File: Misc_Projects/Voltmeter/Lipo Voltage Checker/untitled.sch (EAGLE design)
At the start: 23 parts, among them IC3 ICL7660CPA

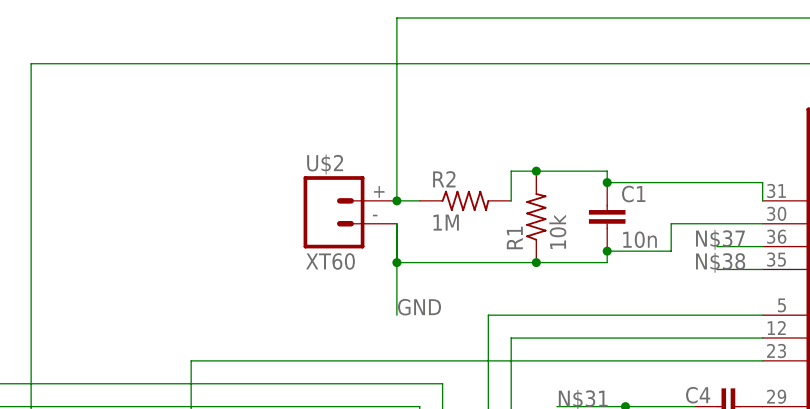
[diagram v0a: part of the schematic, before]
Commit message: Updated to 7mil trace instead of 5mil
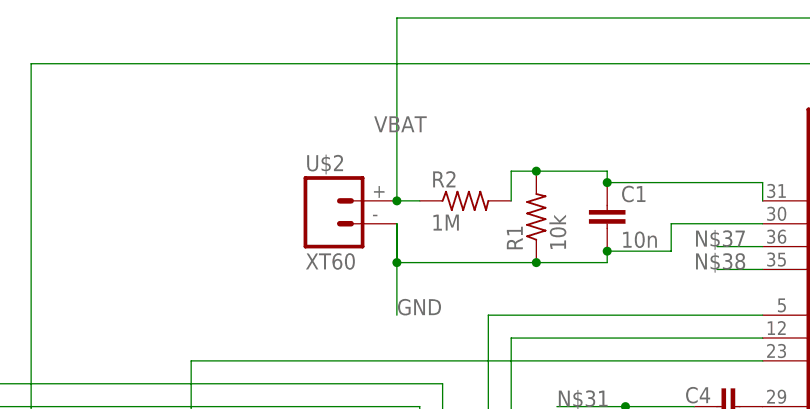
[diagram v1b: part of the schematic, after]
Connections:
- net N$1 renamed VBAT
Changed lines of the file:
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@@
 </busses>
 <nets>
-<net name="N$1" class="0">
+<net name="VBAT" class="0">
 <segment>
 <wire x1="5.08" y1="127" x2="111.76" y2="127" width="0.1524" layer="91"/>
@@
 <wire x1="5.08" y1="127" x2="5.08" y2="106.68" width="0.1524" layer="91"/>
 <junction x="5.08" y="106.68"/>
+<label x="2.54" y="114.3" size="1.778" layer="95"/>
 </segment>
 </net>
